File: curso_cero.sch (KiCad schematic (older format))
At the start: 24 parts, among them P1 CONN_01X06, P2 CONN_01X06, P3 CONN_01X03, P4 CONN_01X04, P5 CONN_01X03, P6 CONN_01X03, P7 CONN_01X08, P8 CONN_01X08, P9 CONN_01X04, SW1 SW_PUSH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

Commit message: Cambios para las nuevas versiones de Kicad. Corregidos fallos estéticos
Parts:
- D1, D2, D3: symbol LED -> LED-RESCUE-curso_cero
- R1, R2, R3, R4, R5, R6, R7: symbol R -> R-RESCUE-curso_cero
- RV1, RV2: symbol POT -> POT-RESCUE-curso_cero
- SW1, SW2: footprint Discret:SW_PUSH_SMALL -> Buttons_Switches_ThroughHole:SW_PUSH_SMALL
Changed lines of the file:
@@
 EESchema Schematic File Version 2
+LIBS:curso_cero-rescue
 LIBS:power
 LIBS:device
@@
 LIBS:memory
 LIBS:xilinx
-LIBS:special
 LIBS:microcontrollers
 LIBS:dsp
@@
 $EndDescr
 $Comp
-L R R3
+L R-RESCUE-curso_cero R3
 U 1 1 54BE44FE
 P 3750 2500
@@
 $EndComp
 $Comp
-L LED D2
+L LED-RESCUE-curso_cero D2
 U 1 1 54BE44FF
 P 3750 3100
@@
 PIN12
 $Comp
-L R R5
+L R-RESCUE-curso_cero R5
 U 1 1 54BE45E3
 P 4400 2500
@@
 $EndComp
 $Comp
-L LED D3
+L LED-RESCUE-curso_cero D3
 U 1 1 54BE466A
 P 4400 3100
@@
 $EndComp
 $Comp
-L POT RV1
+L POT-RESCUE-curso_cero RV1
 U 1 1 54BE4B2B
 P 6150 2650
@@
 	6300 2650 6550 2650
 $Comp
-L POT RV2
+L POT-RESCUE-curso_cero RV2
 U 1 1 54BE4C98
 P 7250 2650
@@
 	7100 3200 7250 3200
 $Comp
-L R R1
+L R-RESCUE-curso_cero R1
 U 1 1 54BE4FDB
 P 3150 2500
@@
 $EndComp
 $Comp
-L LED D1
+L LED-RESCUE-curso_cero D1
 U 1 1 54BE5031
 P 3150 3100
@@
 F 0 "SW1" H 3300 4610 50  0000 C CNN
 F 1 "SW_PUSH" H 3150 4420 50  0000 C CNN
-F 2 "Discret:SW_PUSH_SMALL" H 3150 4500 60  0001 C CNN
+F 2 "Buttons_Switches_ThroughHole:SW_PUSH_SMALL" H 3150 4500 60  0001 C CNN
 F 3 "" H 3150 4500 60  0000 C CNN
 	1    3150 4500
@@
 $EndComp
 $Comp
-L R R2
+L R-RESCUE-curso_cero R2
 U 1 1 54BE57F0
 P 3150 5250
@@
 $EndComp
 $Comp
-L R R4
+L R-RESCUE-curso_cero R4
 U 1 1 54BE584B
 P 4250 5250
@@
 F 0 "SW2" H 4400 4610 50  0000 C CNN
 F 1 "SW_PUSH" H 4250 4420 50  0000 C CNN
-F 2 "Discret:SW_PUSH_SMALL" H 4250 4500 60  0001 C CNN
+F 2 "Buttons_Switches_ThroughHole:SW_PUSH_SMALL" H 4250 4500 60  0001 C CNN
 F 3 "" H 4250 4500 60  0000 C CNN
 	1    4250 4500
@@
 	4250 5500 4250 5700
 $Comp
-L R R6
+L R-RESCUE-curso_cero R6
 U 1 1 54BE6119
 P 5400 4450
@@
 $EndComp
 $Comp
-L R R7
+L R-RESCUE-curso_cero R7
 U 1 1 54BE6161
 P 5400 5250

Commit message: cambiados footprints por reemplazos de nueva librería kicad
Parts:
- D1, D2, D3: footprint LEDs:LED-5MM -> LEDs:LED_D5.0mm
- P1, P2: footprint Pin_Headers:Pin_Header_Straight_1x06 -> Pin_Headers:Pin_Header_Straight_1x06_Pitch2.54mm
- P3: footprint Socket_Strips:Socket_Strip_Straight_1x03 -> Socket_Strips:Socket_Strip_Straight_1x03_Pitch2.54mm
- P4, P9: footprint Socket_Strips:Socket_Strip_Straight_1x04 -> Socket_Strips:Socket_Strip_Straight_1x04_Pitch2.54mm
- P5, P6: footprint Pin_Headers:Pin_Header_Straight_1x03 -> Pin_Headers:Pin_Header_Straight_1x03_Pitch2.54mm
- P7, P8: footprint Pin_Headers:Pin_Header_Straight_1x08 -> Pin_Headers:Pin_Header_Straight_1x08_Pitch2.54mm
- R1, R2, R3, R4, R5, R7: footprint Discret:R3 -> Resistors_ThroughHole:R_Axial_DIN0207_L6.3mm_D2.5mm_P7.62mm_Horizontal
- R6: footprint Discret:R1 -> Opto-Devices:Resistor_LDR_4.9x4.2_RM2.54
- RV1, RV2: footprint Pin_Headers:Pin_Header_Straight_1x03 -> Potentiometers:Potentiometer_Alps_RK09K_Horizontal
- SW1, SW2: footprint Buttons_Switches_ThroughHole:SW_PUSH_SMALL -> Buttons_Switches_ThroughHole:SW_PUSH_6mm_h5mm
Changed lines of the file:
@@
 EESchema Schematic File Version 2
-LIBS:curso_cero-rescue
 LIBS:power
 LIBS:device
@@
 F 0 "R3" V 3830 2500 50  0000 C CNN
 F 1 "330R" V 3757 2501 50  0000 C CNN
-F 2 "Discret:R3" V 3680 2500 30  0001 C CNN
+F 2 "Resistors_ThroughHole:R_Axial_DIN0207_L6.3mm_D2.5mm_P7.62mm_Horizontal" V 3680 2500 30  0001 C CNN
 F 3 "" H 3750 2500 30  0000 C CNN
 	1    3750 2500
@@
 F 0 "D2" H 3750 3200 50  0000 C CNN
 F 1 "LED" H 3750 3000 50  0000 C CNN
-F 2 "LEDs:LED-5MM" H 3750 3100 60  0001 C CNN
+F 2 "LEDs:LED_D5.0mm" H 3750 3100 60  0001 C CNN
 F 3 "" H 3750 3100 60  0000 C CNN
 	1    3750 3100
@@
 F 0 "P1" H 1200 2350 50  0000 C CNN
 F 1 "CONN_01X06" V 1300 2000 50  0000 C CNN
-F 2 "Pin_Headers:Pin_Header_Straight_1x06" H 1200 2000 60  0001 C CNN
+F 2 "Pin_Headers:Pin_Header_Straight_1x06_Pitch2.54mm" H 1200 2000 60  0001 C CNN
 F 3 "" H 1200 2000 60  0000 C CNN
 	1    1200 2000
@@
 F 0 "R5" V 4480 2500 50  0000 C CNN
 F 1 "330R" V 4407 2501 50  0000 C CNN
-F 2 "Discret:R3" V 4330 2500 30  0001 C CNN
+F 2 "Resistors_ThroughHole:R_Axial_DIN0207_L6.3mm_D2.5mm_P7.62mm_Horizontal" V 4330 2500 30  0001 C CNN
 F 3 "" H 4400 2500 30  0000 C CNN
 	1    4400 2500
@@
 F 0 "D3" H 4400 3200 50  0000 C CNN
 F 1 "LED" H 4400 3000 50  0000 C CNN
-F 2 "LEDs:LED-5MM" H 4400 3100 60  0001 C CNN
+F 2 "LEDs:LED_D5.0mm" H 4400 3100 60  0001 C CNN
 F 3 "" H 4400 3100 60  0000 C CNN
 	1    4400 3100
@@
 F 0 "RV1" H 6150 2550 50  0000 C CNN
 F 1 "POT" H 6150 2650 50  0000 C CNN
-F 2 "Pin_Headers:Pin_Header_Straight_1x03" H 6150 2650 60  0001 C CNN
+F 2 "Potentiometers:Potentiometer_Alps_RK09K_Horizontal" H 6150 2650 60  0001 C CNN
 F 3 "" H 6150 2650 60  0000 C CNN
 	1    6150 2650
@@
 F 0 "RV2" H 7250 2550 50  0000 C CNN
 F 1 "POT" H 7250 2650 50  0000 C CNN
-F 2 "Pin_Headers:Pin_Header_Straight_1x03" H 7250 2650 60  0001 C CNN
+F 2 "Potentiometers:Potentiometer_Alps_RK09K_Horizontal" H 7250 2650 60  0001 C CNN
 F 3 "" H 7250 2650 60  0000 C CNN
 	1    7250 2650
@@
 F 0 "R1" V 3230 2500 50  0000 C CNN
 F 1 "330R" V 3157 2501 50  0000 C CNN
-F 2 "Discret:R3" V 3080 2500 30  0001 C CNN
+F 2 "Resistors_ThroughHole:R_Axial_DIN0207_L6.3mm_D2.5mm_P7.62mm_Horizontal" V 3080 2500 30  0001 C CNN
 F 3 "" H 3150 2500 30  0000 C CNN
 	1    3150 2500
@@
 F 0 "D1" H 3150 3200 50  0000 C CNN
 F 1 "LED" H 3150 3000 50  0000 C CNN
-F 2 "LEDs:LED-5MM" H 3150 3100 60  0001 C CNN
+F 2 "LEDs:LED_D5.0mm" H 3150 3100 60  0001 C CNN
 F 3 "" H 3150 3100 60  0000 C CNN
 	1    3150 3100
@@
 F 0 "SW1" H 3300 4610 50  0000 C CNN
 F 1 "SW_PUSH" H 3150 4420 50  0000 C CNN
-F 2 "Buttons_Switches_ThroughHole:SW_PUSH_SMALL" H 3150 4500 60  0001 C CNN
+F 2 "Buttons_Switches_ThroughHole:SW_PUSH_6mm_h5mm" H 3150 4500 60  0001 C CNN
 F 3 "" H 3150 4500 60  0000 C CNN
 	1    3150 4500
@@
 F 0 "R2" V 3230 5250 50  0000 C CNN
 F 1 "10K" V 3157 5251 50  0000 C CNN
-F 2 "Discret:R3" V 3080 5250 30  0001 C CNN
+F 2 "Resistors_ThroughHole:R_Axial_DIN0207_L6.3mm_D2.5mm_P7.62mm_Horizontal" V 3080 5250 30  0001 C CNN
 F 3 "" H 3150 5250 30  0000 C CNN
 	1    3150 5250
@@
 F 0 "R4" V 4330 5250 50  0000 C CNN
 F 1 "10K" V 4257 5251 50  0000 C CNN
-F 2 "Discret:R3" V 4180 5250 30  0001 C CNN
+F 2 "Resistors_ThroughHole:R_Axial_DIN0207_L6.3mm_D2.5mm_P7.62mm_Horizontal" V 4180 5250 30  0001 C CNN
 F 3 "" H 4250 5250 30  0000 C CNN
 	1    4250 5250
@@
 F 0 "SW2" H 4400 4610 50  0000 C CNN
 F 1 "SW_PUSH" H 4250 4420 50  0000 C CNN
-F 2 "Buttons_Switches_ThroughHole:SW_PUSH_SMALL" H 4250 4500 60  0001 C CNN
+F 2 "Buttons_Switches_ThroughHole:SW_PUSH_6mm_h5mm" H 4250 4500 60  0001 C CNN
 F 3 "" H 4250 4500 60  0000 C CNN
 	1    4250 4500
@@
 F 0 "R6" V 5480 4450 50  0000 C CNN
 F 1 "LDR" V 5407 4451 50  0000 C CNN
-F 2 "Discret:R1" V 5330 4450 30  0001 C CNN
+F 2 "Opto-Devices:Resistor_LDR_4.9x4.2_RM2.54" V 5330 4450 30  0001 C CNN
 F 3 "" H 5400 4450 30  0000 C CNN
 	1    5400 4450
@@
 F 0 "R7" V 5480 5250 50  0000 C CNN
 F 1 "10K" V 5407 5251 50  0000 C CNN
-F 2 "Discret:R3" V 5330 5250 30  0001 C CNN
+F 2 "Resistors_ThroughHole:R_Axial_DIN0207_L6.3mm_D2.5mm_P7.62mm_Horizontal" V 5330 5250 30  0001 C CNN
 F 3 "" H 5400 5250 30  0000 C CNN
 	1    5400 5250
@@
 F 0 "P2" H 1200 3350 50  0000 C CNN
 F 1 "CONN_01X06" V 1300 3000 50  0000 C CNN
-F 2 "Pin_Headers:Pin_Header_Straight_1x06" H 1200 3000 60  0001 C CNN
+F 2 "Pin_Headers:Pin_Header_Straight_1x06_Pitch2.54mm" H 1200 3000 60  0001 C CNN
 F 3 "" H 1200 3000 60  0000 C CNN
 	1    1200 3000
@@
 F 0 "P7" H 10450 2450 50  0000 C CNN
 F 1 "CONN_01X08" V 10550 2000 50  0000 C CNN
-F 2 "Pin_Headers:Pin_Header_Straight_1x08" H 10450 2000 60  0001 C CNN
+F 2 "Pin_Headers:Pin_Header_Straight_1x08_Pitch2.54mm" H 10450 2000 60  0001 C CNN
 F 3 "" H 10450 2000 60  0000 C CNN
 	1    10450 2000
@@
 F 0 "P8" H 10450 3700 50  0000 C CNN
 F 1 "CONN_01X08" V 10550 3250 50  0000 C CNN
-F 2 "Pin_Headers:Pin_Header_Straight_1x08" H 10450 3250 60  0001 C CNN
+F 2 "Pin_Headers:Pin_Header_Straight_1x08_Pitch2.54mm" H 10450 3250 60  0001 C CNN
 F 3 "" H 10450 3250 60  0000 C CNN
 	1    10450 3250
@@
 F 0 "P5" H 7000 4950 50  0000 C CNN
 F 1 "CONN_01X03" V 7100 4750 50  0000 C CNN
-F 2 "Pin_Headers:Pin_Header_Straight_1x03" H 7000 4750 60  0001 C CNN
+F 2 "Pin_Headers:Pin_Header_Straight_1x03_Pitch2.54mm" H 7000 4750 60  0001 C CNN
 F 3 "" H 7000 4750 60  0000 C CNN
 	1    7000 4750
@@
 F 0 "P6" H 8650 4950 50  0000 C CNN
 F 1 "CONN_01X03" V 8750 4750 50  0000 C CNN
-F 2 "Pin_Headers:Pin_Header_Straight_1x03" H 8650 4750 60  0001 C CNN
+F 2 "Pin_Headers:Pin_Header_Straight_1x03_Pitch2.54mm" H 8650 4750 60  0001 C CNN
 F 3 "" H 8650 4750 60  0000 C CNN
 	1    8650 4750
@@
 F 0 "P3" H 4100 1100 50  0000 C CNN
 F 1 "CONN_01X03" V 4200 900 50  0000 C CNN
-F 2 "Socket_Strips:Socket_Strip_Straight_1x03" H 4100 900 60  0001 C CNN
+F 2 "Socket_Strips:Socket_Strip_Straight_1x03_Pitch2.54mm" H 4100 900 60  0001 C CNN
 F 3 "" H 4100 900 60  0000 C CNN
 	1    4100 900
@@
 F 0 "P4" H 5700 1150 50  0000 C CNN
 F 1 "CONN_01X04" V 5800 900 50  0000 C CNN
-F 2 "Socket_Strips:Socket_Strip_Straight_1x04" H 5700 900 60  0001 C CNN
+F 2 "Socket_Strips:Socket_Strip_Straight_1x04_Pitch2.54mm" H 5700 900 60  0001 C CNN
 F 3 "" H 5700 900 60  0000 C CNN
 	1    5700 900
@@
 F 0 "P9" H 7200 1000 50  0000 C CNN
 F 1 "CONN_01X04" V 7300 750 50  0000 C CNN
-F 2 "Socket_Strips:Socket_Strip_Straight_1x04" H 7200 750 60  0001 C CNN
+F 2 "Socket_Strips:Socket_Strip_Straight_1x04_Pitch2.54mm" H 7200 750 60  0001 C CNN
 F 3 "" H 7200 750 60  0000 C CNN
 	1    7200 750

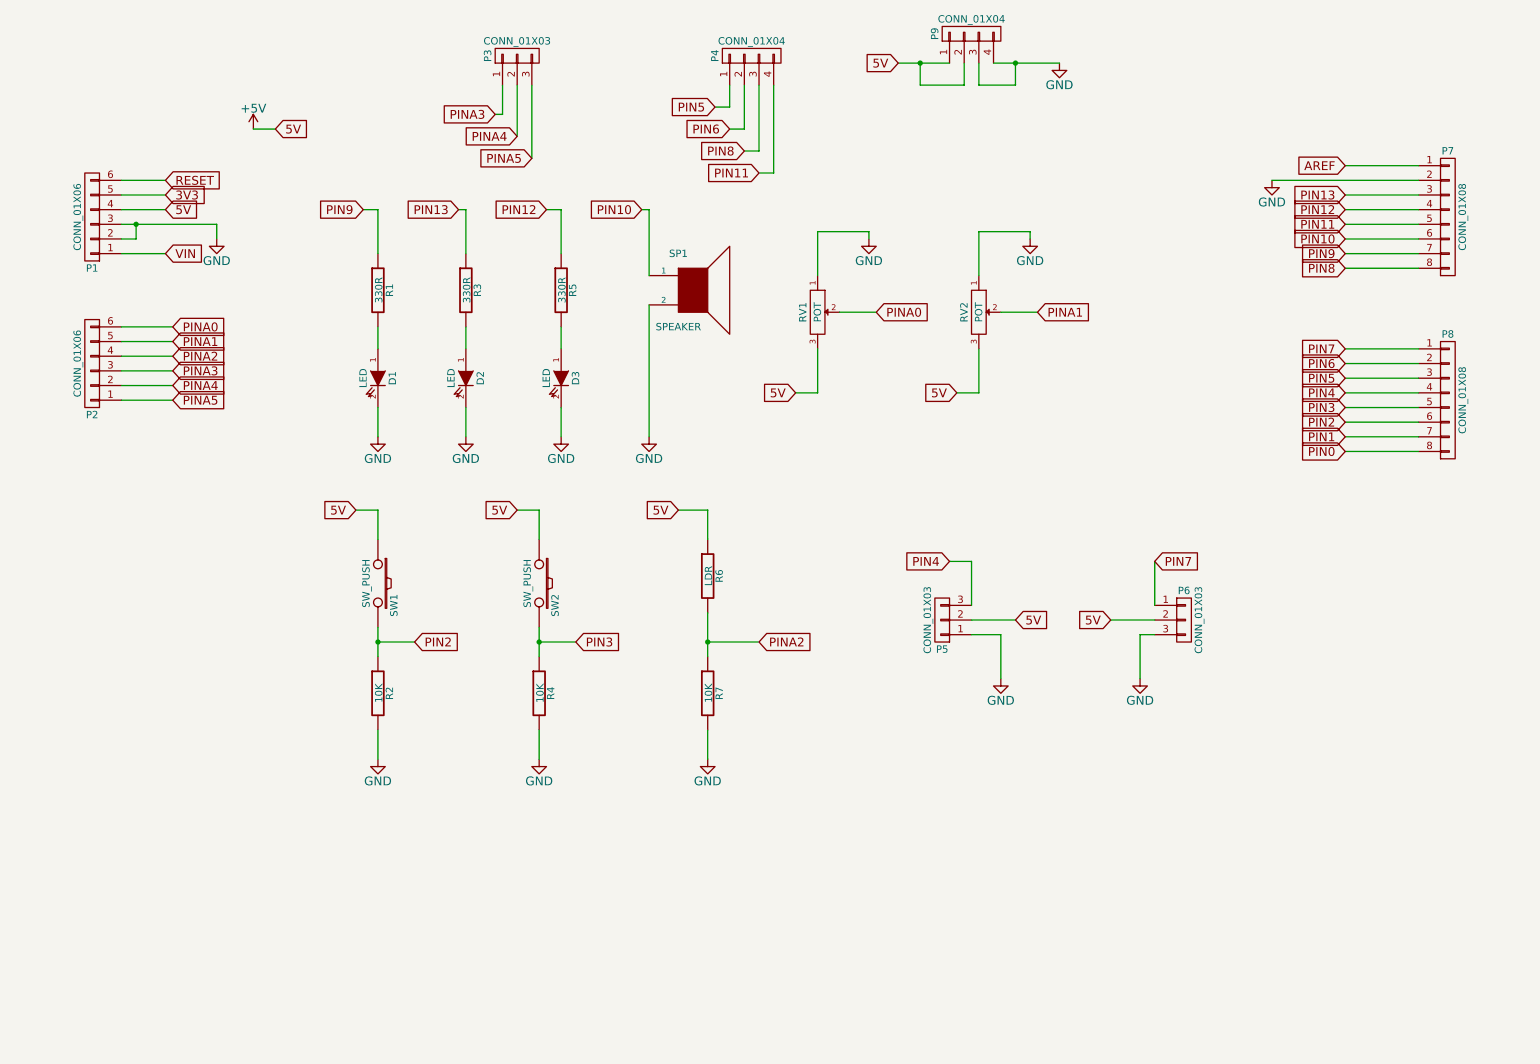
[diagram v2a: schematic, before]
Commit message: recolocado esquematico, corregida polaridad de conectores y buzzer
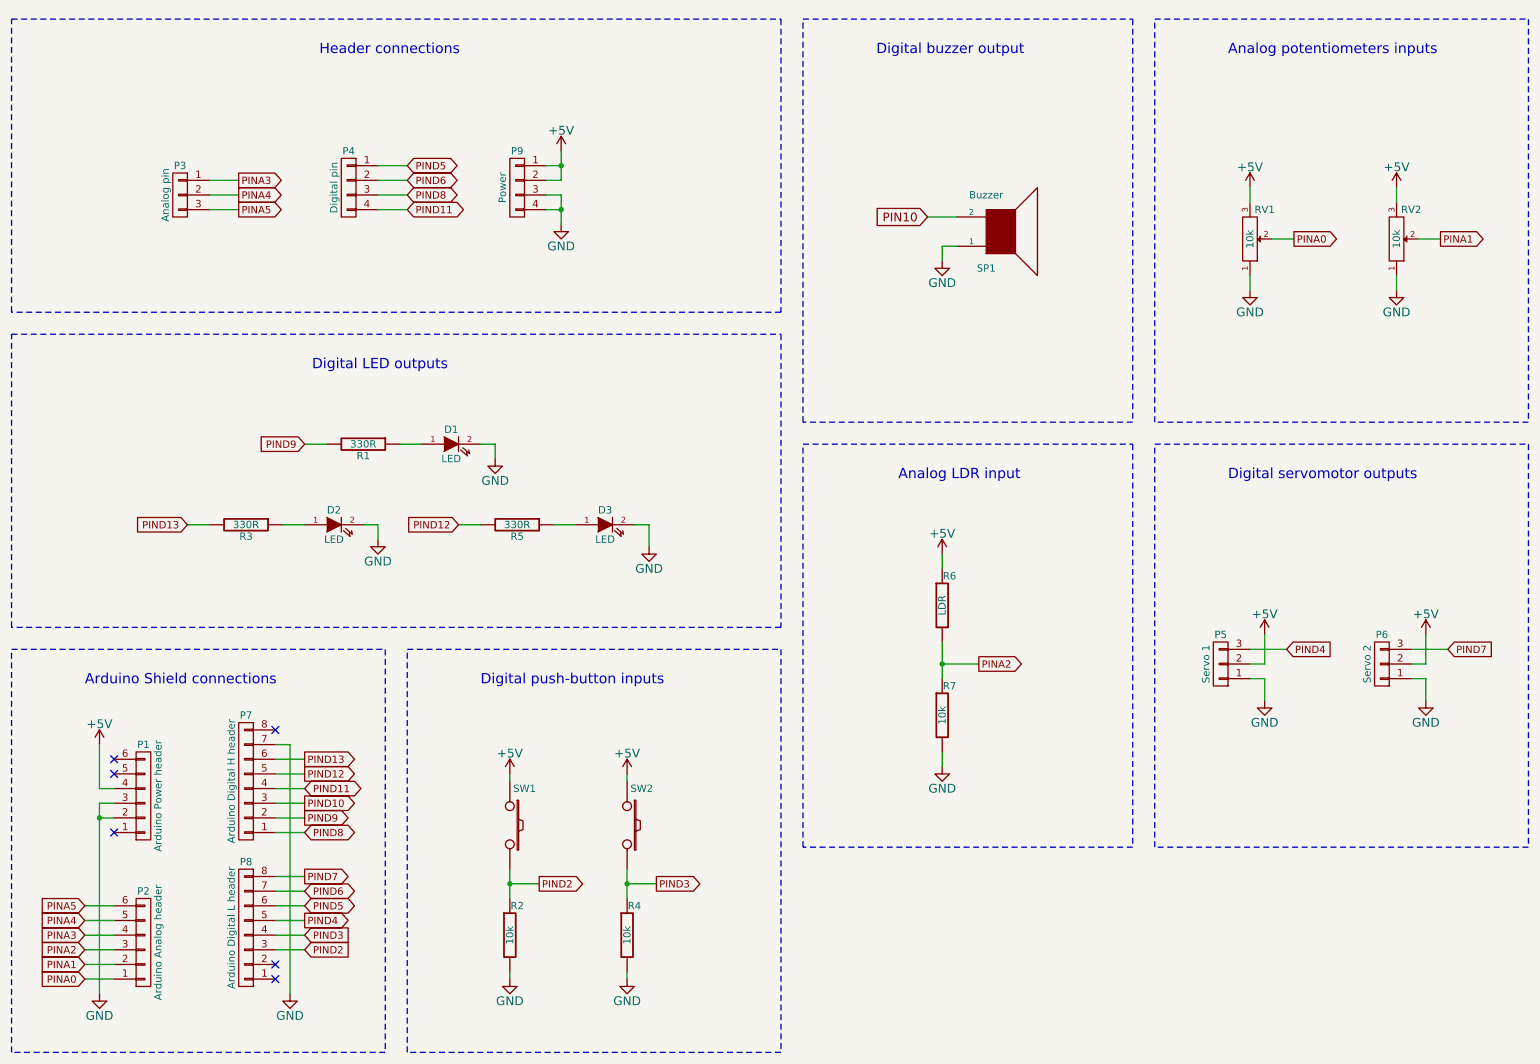
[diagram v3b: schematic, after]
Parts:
- P1: value CONN_01X06 -> Arduino Power header
- P2: value CONN_01X06 -> Arduino Analog header
- P3: value CONN_01X03 -> Analog pin
- P4: value CONN_01X04 -> Digital pin
- P5: value CONN_01X03 -> Servo 1
- P6: value CONN_01X03 -> Servo 2
- P7: value CONN_01X08 -> Arduino Digital H header
- P8: value CONN_01X08 -> Arduino Digital L header
- P9: value CONN_01X04 -> Power
- R2, R4, R7: value 10K -> 10k
- RV1, RV2: value POT -> 10k
- SP1: value SPEAKER -> Buzzer
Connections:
- net GND: now also P6.1 (P1), P7.7 (P7), SP1.1; no longer P6.3 (P3), P7.2 (P2), SP1.2
- net PIN10: now also SP1.2; no longer P7.6 (P6), SP1.1
- net PINA0: now also P2.1 (P1); no longer P2.6 (P6)
- net PINA1: now also P2.2 (P2); no longer P2.5 (P5)
- net PINA2: now also P2.3 (P3); no longer P2.4 (P4)
- net PINA3: now also P2.4 (P4); no longer P2.3 (P3)
- net PINA4: now also P2.5 (P5); no longer P2.2 (P2)
- net PINA5: now also P2.6 (P6); no longer P2.1 (P1)
- net at D2.1 (A): now also R3.1; no longer R3.2
- net at D3.1 (A): now also R5.1; no longer R5.2
- net at D1.1 (A): now also R1.1; no longer R1.2
- net 3V3: no longer names the net of P1.5 (P5)
- net AREF renamed PIND8
- net PIND8: now also P4.3 (P3)
- net PIN0 renamed PIND7
- net PIND7: now also P6.3 (P3)
- net PIN1 renamed PIND6
- net PIND6: now also P4.2 (P2)
- net PIN11 renamed PIND11
- net PIND11: now also P7.4 (P4); no longer P7.5 (P5)
- removed net PIN12: P7.4 (P4), R5.1
- net PIN13 renamed PIND10
- net PIND10: no longer R3.1
- net PIN2 renamed PIND2
- net PIND2: now also P8.3 (P3); no longer P8.6 (P6)
- net PIN3 renamed PIND3
- net PIND3: now also P8.4 (P4); no longer P8.5 (P5)
- net PIN4 renamed PIND4
- net PIND4: now also P8.5 (P5); no longer P8.4 (P4)
- net PIN5 renamed PIND5
- net PIND5: now also P8.6 (P6); no longer P8.3 (P3)
- net PIN6: no longer names the net of P8.2 (P2)
- net PIN6: no longer P4.2 (P2)
- net PIN7: no longer names the net of P8.1 (P1)
- net PIN7: no longer P6.1 (P1)
- net PIN8: no longer names the net of P7.8 (P8)
- net PIN8: no longer P4.3 (P3)
- removed net PIN9: P7.7 (P7), R1.1
- net RESET: no longer names the net of P1.6 (P6)
- net VIN: no longer names the net of P1.1 (P1)
- new net PIND12: P7.5 (P5), R5.2
- new net PIND13: P7.6 (P6), R3.2
- new net PIND9: P7.2 (P2), R1.2
- no-connect marks 0 -> 6
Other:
- note added: "Analog LDR input"
- note added: "Analog potentiometers inputs"
- note added: "Arduino Shield connections"
- note added: "Digital LED outputs"
- note added: "Digital buzzer output"
- note added: "Digital push-button inputs"
- note added: "Digital servomotor outputs"
- note added: "Header connections"
- moved on the sheet: D1, D2, D3, P1, P2, P3, P4, P5, P6, P7, P8, P9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
